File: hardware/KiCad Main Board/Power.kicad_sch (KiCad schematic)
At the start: 53 parts, among them J7 BATT_CONN, Q2 AO3401A, Q3 AO3400A, Q4 AO3400A, Q5 AO3400A, Q6 AO3400A, U10 LM5157RTER, U13 NCP1117-1.8_SOT223, U2 S-8252ACP-M6T1U, U3 NCP1117-3.3_SOT223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

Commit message: working on PCB
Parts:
- removed D5, D6, D7: 30BQ040TRPBF, symbol Device:D_Small
- removed J7: BATT_CONN, symbol Connector:Conn_01x03_Socket
- removed R10, R12: 0, symbol Device:R
- added BT1: BK-18650-PC4, BK-18650-PC4:BAT_BK-18650-PC4, symbol BK-18650-PC4:BK-18650-PC4
- added D30, D54, D55: B340, Diode_SMD:D_SMC, symbol Diode:B340
- added TP5: V_CHG, symbol Connector:TestPoint
- added TP6, TP7: TestPoint, symbol Connector:TestPoint
- D26: footprint (none) -> Diode_SMD:D_0603_1608Metric_Pad1.05x0.95mm_HandSolder
- L3: footprint (none) -> Inductor_SMD:L_APV_APH0650
- R25: footprint (none) -> Resistor_SMD:R_1206_3216Metric_Pad1.30x1.75mm_HandSolder
- R26, R27, R28, R29, R30, R31, R32, R33, R34, R35, R36, R37, R38, R39, R49: footprint (none) -> Resistor_SMD:R_0603_1608Metric_Pad0.98x0.95mm_HandSolder
- U10: footprint QFN_57RTER_TEX -> LM5157:QFN_57RTER_TEX-M
- U2: footprint SOT236-A-PKG_MP006-A-P-SD-2.1_ABL -> S-8252:SOT236-A-PKG_MP006-A-P-SD-2.1_ABL
- U9: value MCP73844-840I/MS -> MCP73844-820I/MS; footprint MSOP8_MC_MCH -> MCP73844:MSOP8_MC_MCH-M
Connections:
- net 1V8_AUDIO: now also TP7.1
- net 3V3_MCU: now also TP6.1
- net 5V_USB: now also D30.2 (A)
- net GND: now also C48.1, C5.1, C50.1, C6.1
- net V_BAT: now also C5.2, C50.2, C63.2, C64.2, U13.3 (VI), U3.3 (VI)
- net V_BAT_RAW: now also BT1.1+
- net V_CHG: now also D54.1 (K), TP5.1
- net at L3.2, U10.12 (SW), U10.13 (SW)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: now also D54.2 (A)
- net at R25.2, U9.1 (SENSE): now also D55.2 (A)
- net at R31.2, R35.1: now also BT1.1-, BT1.2+
- net at C56.2, Q3.2 (S), Q5.2 (S)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: now also BT1.2-
- net at C51.2, C52.2, C58.1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: now also D30.1 (K)
- net at Q2.2 (S): now also D55.1 (K)

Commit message: all GPIO nets connected on schematic
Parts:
- added TP30: TestPoint, TestPoint:TestPoint_Pad_D1.0mm, symbol Connector:TestPoint
- TP5, TP6, TP7: footprint (none) -> TestPoint:TestPoint_Pad_D1.0mm
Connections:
- net V_BAT_RAW: now also TP30.1
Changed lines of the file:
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@@
 	)
 	(junction
+		(at 173.99 91.44)
+		(diameter 0)
+		(color 0 0 0 0)
+	)
+	(junction
 		(at 135.89 69.85)
 		(diameter 0)
@@
 	(wire
 		(pts
+			(xy 173.99 91.44) (xy 250.19 91.44)
+		)
+		(stroke
+			(width 0)
+			(type default)
+		)
+	)
+	(wire
+		(pts
 			(xy 223.52 25.4) (xy 229.87 25.4)
 		)
@@
 	(wire
 		(pts
-			(xy 142.24 91.44) (xy 250.19 91.44)
+			(xy 142.24 91.44) (xy 173.99 91.44)
 		)
 		(stroke
@@
 			)
 		)
-		(property "Footprint" ""
+		(property "Footprint" "TestPoint:TestPoint_Pad_D1.0mm"
 			(at 38.1 91.44 0)
 			(effects
@@
 			)
 		)
-		(property "Footprint" ""
+		(property "Footprint" "TestPoint:TestPoint_Pad_D1.0mm"
 			(at 267.97 52.07 0)
 			(effects
@@
 			)
 		)
-		(property "Footprint" ""
+		(property "Footprint" "TestPoint:TestPoint_Pad_D1.0mm"
 			(at 270.51 25.4 0)
 			(effects
@@
 					(unit 1)
 				)
+			)
+		)
+	)
+	(symbol
+		(lib_id "Connector:TestPoint")
+		(at 173.99 91.44 0)
+		(unit 1)
+		(exclude_from_sim no)
+		(in_bom yes)
+		(on_board yes)
+		(dnp no)
+		(property "Reference" "TP30"
+			(at 173.228 89.408 0)
+			(effects
+				(font
+					(size 1.27 1.27)
+				)
+				(justify right)
+			)
+		)
+		(property "Value" "TestPoint"
+			(at 173.228 87.376 0)
+			(effects
+				(font
+					(size 1.27 1.27)
+				)
+				(justify right)
+			)
+		)
+		(property "Footprint" "TestPoint:TestPoint_Pad_D1.0mm"
+			(at 179.07 91.44 0)
+			(effects
+				(font
+					(size 1.27 1.27)
+				)
+				(hide yes)
+			)
+		)
+		(property "Datasheet" "~"
+			(at 179.07 91.44 0)
+			(effects
+				(font
+					(size 1.27 1.27)
+				)
+				(hide yes)
+			)
+		)
+		(property "Description" "test point"
+			(at 173.99 91.44 0)
+			(effects
+				(font
+					(size 1.27 1.27)
+				)
+				(hide yes)
+			)
+		)
+		(pin "1"
+		)
+		(instances
+			(project "OSS Radio Hardware Design"
+				(path "/fd5c68a7-f5d0-4135-a258-bde3ebf63307/c701d20d-e266-4c46-aeb3-ff3d813a359d"
+					(reference "TP30")
+					(unit 1)
+				)

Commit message: mostly designed PCB
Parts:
- removed TP6, TP7: TestPoint, TestPoint:TestPoint_Pad_D1.0mm, symbol Connector:TestPoint
- added C78: 4.7u, Capacitor_SMD:C_0603_1608Metric_Pad1.08x0.95mm_HandSolder, symbol Device:C
- D30, D54, D55: footprint Diode_SMD:D_SMC -> Diode_SMD:D_SMA
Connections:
- net 1V8_AUDIO: now also C78.2
- net GND: now also C78.1
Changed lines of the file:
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@@
 	)
 	(junction
+		(at 266.7 52.07)
+		(diameter 0)
+		(color 0 0 0 0)
+	)
+	(junction
 		(at 46.99 106.68)
 		(diameter 0)
@@
 	)
 	(junction
-		(at 36.83 69.85)
+		(at 256.54 59.69)
 		(diameter 0)
 		(color 0 0 0 0)
 	)
 	(junction
-		(at 222.25 137.16)
+		(at 36.83 69.85)
 		(diameter 0)
 		(color 0 0 0 0)
 	)
 	(junction
-		(at 262.89 52.07)
+		(at 222.25 137.16)
 		(diameter 0)
 		(color 0 0 0 0)
@@
 	)
 	(junction
-		(at 265.43 25.4)
-		(diameter 0)
-		(color 0 0 0 0)
-	)
-	(junction
 		(at 208.28 40.64)
 		(diameter 0)
@@
 	(wire
 		(pts
-			(xy 256.54 25.4) (xy 265.43 25.4)
+			(xy 256.54 25.4) (xy 267.97 25.4)
 		)
 		(stroke
@@
 	(wire
 		(pts
-			(xy 265.43 25.4) (xy 267.97 25.4)
-		)
-		(stroke
-			(width 0)
-			(type default)
-		)
-	)
-	(wire
-		(pts
 			(xy 52.07 109.22) (xy 43.18 109.22)
 		)
@@
 	(wire
 		(pts
-			(xy 256.54 52.07) (xy 262.89 52.07)
-		)
-		(stroke
-			(width 0)
-			(type default)
-		)
-	)
-	(wire
-		(pts
 			(xy 36.83 106.68) (xy 36.83 109.22)
 		)
@@
 	(wire
 		(pts
-			(xy 262.89 52.07) (xy 267.97 52.07)
+			(xy 256.54 52.07) (xy 266.7 52.07)
 		)
 		(stroke
@@
 	(wire
 		(pts
+			(xy 256.54 59.69) (xy 266.7 59.69)
+		)
+		(stroke
+			(width 0)
+			(type default)
+		)
+	)
+	(wire
+		(pts
 			(xy 69.85 55.88) (xy 68.58 55.88)
 		)
@@
 	(wire
 		(pts
+			(xy 266.7 52.07) (xy 267.97 52.07)
+		)
+		(stroke
+			(width 0)
+			(type default)
+		)
+	)
+	(wire
+		(pts
 			(xy 223.52 33.02) (xy 223.52 34.29)
 		)
@@
 	)
 	(symbol
+		(lib_id "Device:C")
+		(at 266.7 55.88 180)
+		(unit 1)
+		(exclude_from_sim no)
+		(in_bom yes)
+		(on_board yes)
+		(dnp no)
+		(fields_autoplaced yes)
+		(property "Reference" "C78"
+			(at 270.51 54.6099 0)
+			(effects
+				(font
+					(size 1.27 1.27)
+				)
+				(justify right)
+			)
+		)
+		(property "Value" "4.7u"
+			(at 270.51 57.1499 0)
+			(effects
+				(font
+					(size 1.27 1.27)
+				)
+				(justify right)
+			)
+		)
+		(property "Footprint" "Capacitor_SMD:C_0603_1608Metric_Pad1.08x0.95mm_HandSolder"
+			(at 265.7348 52.07 0)
+			(effects
+				(font
+					(size 1.27 1.27)
+				)
+				(hide yes)
+			)
+		)
+		(property "Datasheet" "~"
+			(at 266.7 55.88 0)
+			(effects
+				(font
+					(size 1.27 1.27)
+				)
+				(hide yes)
+			)
+		)
+		(property "Description" "Unpolarized capacitor"
+			(at 266.7 55.88 0)
+			(effects
+				(font
+					(size 1.27 1.27)
+				)
+				(hide yes)
+			)
+		)
+		(pin "1"
+		)
+		(pin "2"
+		)
+		(instances
+			(project "OSS Radio Hardware Design"
+				(path "/fd5c68a7-f5d0-4135-a258-bde3ebf63307/c701d20d-e266-4c46-aeb3-ff3d813a359d"
+					(reference "C78")
+					(unit 1)
+				)
+			)
+		)
+	)
+	(symbol
 		(lib_id "Device:R_Small")
 		(at 149.86 52.07 0)
@@
 	)
 	(symbol
-		(lib_id "Connector:TestPoint")
-		(at 262.89 52.07 0)
-		(unit 1)
-		(exclude_from_sim no)
-		(in_bom yes)
-		(on_board yes)
-		(dnp no)
-		(fields_autoplaced yes)
-		(property "Reference" "TP7"
-			(at 265.43 47.4979 0)
-			(effects
-				(font
-					(size 1.27 1.27)
-				)
-				(justify left)
-			)
-		)
-		(property "Value" "TestPoint"
-			(at 265.43 50.0379 0)
-			(effects
-				(font
-					(size 1.27 1.27)
-				)
-				(justify left)
-			)
-		)
-		(property "Footprint" "TestPoint:TestPoint_Pad_D1.0mm"
-			(at 267.97 52.07 0)
-			(effects
-				(font
-					(size 1.27 1.27)
-				)
-				(hide yes)
-			)
-		)
-		(property "Datasheet" "~"
-			(at 267.97 52.07 0)
-			(effects
-				(font
-					(size 1.27 1.27)
-				)
-				(hide yes)
-			)
-		)
-		(property "Description" "test point"
-			(at 262.89 52.07 0)
-			(effects
-				(font
-					(size 1.27 1.27)
-				)
-				(hide yes)
-			)
-		)
-		(pin "1"
-		)
-		(instances
-			(project "OSS Radio Hardware Design"
-				(path "/fd5c68a7-f5d0-4135-a258-bde3ebf63307/c701d20d-e266-4c46-aeb3-ff3d813a359d"
-					(reference "TP7")
-					(unit 1)
-				)
-			)
-		)
-	)
-	(symbol
 		(lib_id "Device:R_Small")
 		(at 186.69 111.76 270)
@@
 	)
 	(symbol
-		(lib_id "Connector:TestPoint")
-		(at 265.43 25.4 0)
-		(unit 1)
-		(exclude_from_sim no)
-		(in_bom yes)
-		(on_board yes)
-		(dnp no)
-		(fields_autoplaced yes)
-		(property "Reference" "TP6"
-			(at 267.97 20.8279 0)
-			(effects
-				(font
-					(size 1.27 1.27)
-				)
-				(justify left)
-			)
-		)
-		(property "Value" "TestPoint"
-			(at 267.97 23.3679 0)
-			(effects
-				(font
-					(size 1.27 1.27)
-				)
-				(justify left)
-			)
-		)
-		(property "Footprint" "TestPoint:TestPoint_Pad_D1.0mm"
-			(at 270.51 25.4 0)
-			(effects
-				(font
-					(size 1.27 1.27)
-				)
-				(hide yes)
-			)
-		)
-		(property "Datasheet" "~"
-			(at 270.51 25.4 0)
-			(effects
-				(font
-					(size 1.27 1.27)
-				)
-				(hide yes)
-			)
-		)
-		(property "Description" "test point"
-			(at 265.43 25.4 0)
-			(effects
-				(font
-					(size 1.27 1.27)
-				)
-				(hide yes)
-			)
-		)
-		(pin "1"
-		)
-		(instances
-			(project ""
-				(path "/fd5c68a7-f5d0-4135-a258-bde3ebf63307/c701d20d-e266-4c46-aeb3-ff3d813a359d"
-					(reference "TP6")
-					(unit 1)
-				)
-			)
-		)
-	)
-	(symbol
 		(lib_id "Device:R_Small")
 		(at 41.91 106.68 270)
@@
 			)
 		)
-		(property "Footprint" "Diode_SMD:D_SMC"
+		(property "Footprint" "Diode_SMD:D_SMA"
 			(at 31.75 17.145 0)
 			(effects
@@
 			)
 		)
-		(property "Footprint" "Diode_SMD:D_SMC"
+		(property "Footprint" "Diode_SMD:D_SMA"
 			(at 143.51 41.275 0)
 			(effects
@@
 			)
 		)
-		(property "Footprint" "Diode_SMD:D_SMC"
+		(property "Footprint" "Diode_SMD:D_SMA"
 			(at 96.52 86.995 0)
 			(effects

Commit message: did all the things
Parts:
- added D59: 1N4148WS, Diode_SMD:D_SOD-323, symbol Diode:1N4148WS
- added J9: Batt_Conn, TestPoint:TestPoint_2Pads_Pitch2.54mm_Drill0.8mm, symbol Connector:Conn_01x02_Pin
- BT1, C56, C57, Q3, Q4, R30, R31, R32, R33, R34, R35, U2: now not fitted
- R49: value 100 -> 1k
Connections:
- net 3V3_MCU: no longer D26.2 (A)
- net CHGR_STAT: now also D59.2 (A); no longer R49.2, U9.3 (STAT1)
- net GND: now also J9.1 (Pin_1)
- net V_BAT_RAW: now also J9.2 (Pin_2)
- net V_CHG: now also D26.2 (A)
- new net: D59.1 (K), R49.2, U9.3 (STAT1)
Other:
- moved on the sheet: C59, R28

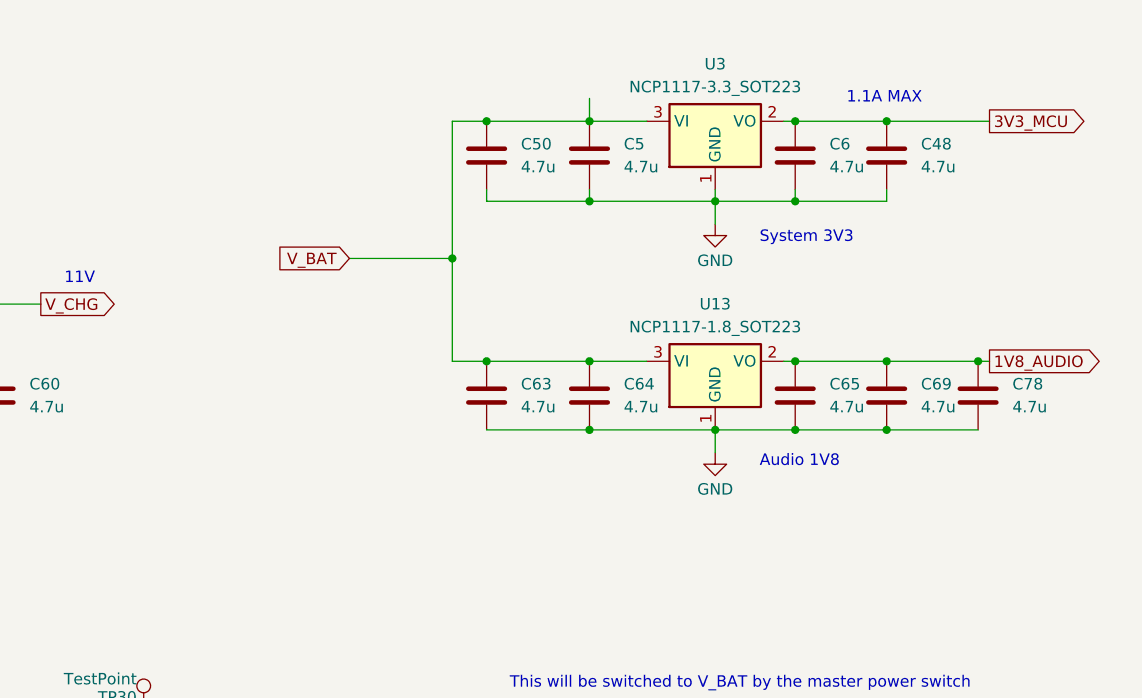
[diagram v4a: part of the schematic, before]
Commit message: changed 3V3 regulator from LDO to switching, updated PCB and minor PCB changes
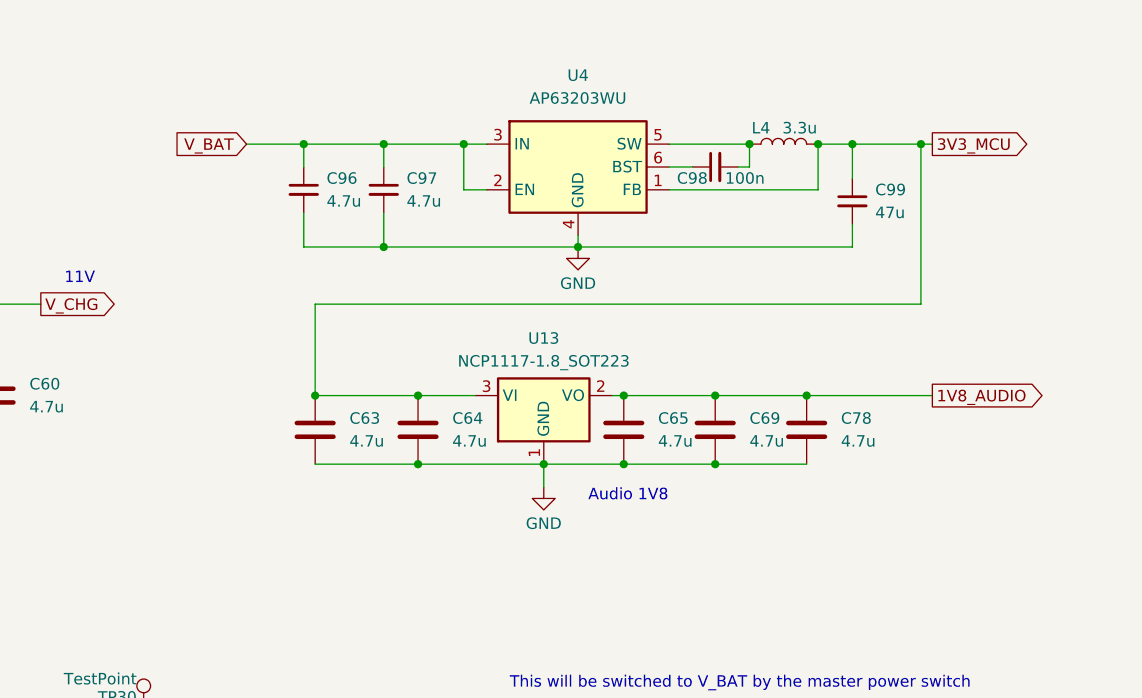
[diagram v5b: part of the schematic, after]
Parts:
- removed C48, C5, C50, C6: 4.7u, Capacitor_SMD:C_0603_1608Metric_Pad1.08x0.95mm_HandSolder, symbol Device:C
- removed U3: NCP1117-3.3_SOT223, Package_TO_SOT_SMD:SOT-223-3_TabPin2, symbol Regulator_Linear:NCP1117-3.3_SOT223
- added C96, C97: 4.7u, Capacitor_SMD:C_0603_1608Metric_Pad1.08x0.95mm_HandSolder, symbol Device:C_Small
- added C98: 100n, Capacitor_SMD:C_0603_1608Metric_Pad1.08x0.95mm_HandSolder, symbol Device:C_Small
- added C99: 47u, Capacitor_SMD:C_1206_3216Metric_Pad1.33x1.80mm_HandSolder, symbol Device:C_Small
- added L4: 3.3u, Inductor_SMD:L_0805_2012Metric_Pad1.15x1.40mm_HandSolder, symbol Device:L
- added U4: AP63203WU, Package_TO_SOT_SMD:TSOT-23-6, symbol Regulator_Switching:AP63203WU
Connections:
- net 3V3_MCU: now also C63.2, C64.2, U13.3 (VI), C99.1, L4.2, U4.1 (FB)
- net GND: now also C96.2, C97.2, C99.2, U4.4 (GND)
- net V_BAT: now also C96.1, C97.1, U4.2 (EN), U4.3 (IN); no longer C63.2, C64.2, U13.3 (VI)
- new net: C98.1, U4.6 (BST)
- new net: C98.2, L4.1, U4.5 (SW)
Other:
- note removed: "1.1A MAX"
- note removed: "System 3V3"
- moved on the sheet: C63, C64, C65, C69, C78, U13

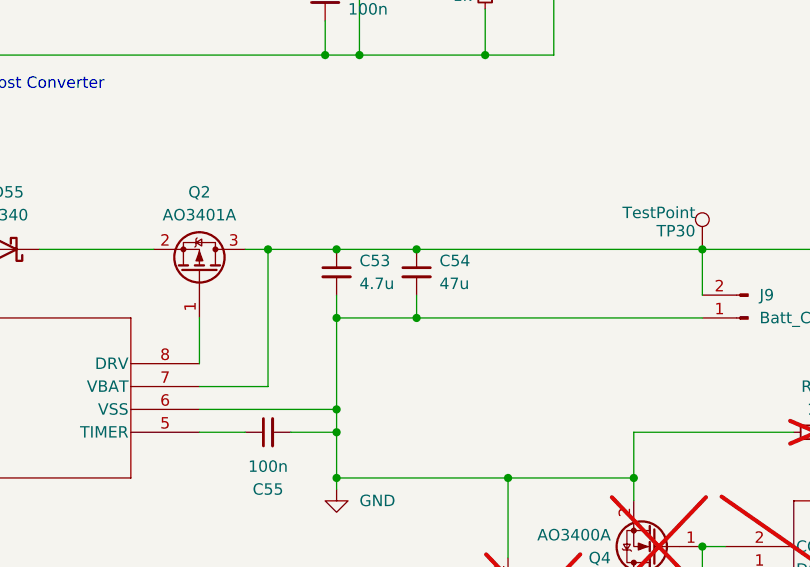
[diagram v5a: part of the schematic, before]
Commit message: changed charge output 47uF cap to 4.7uF due to size/voltage constraints
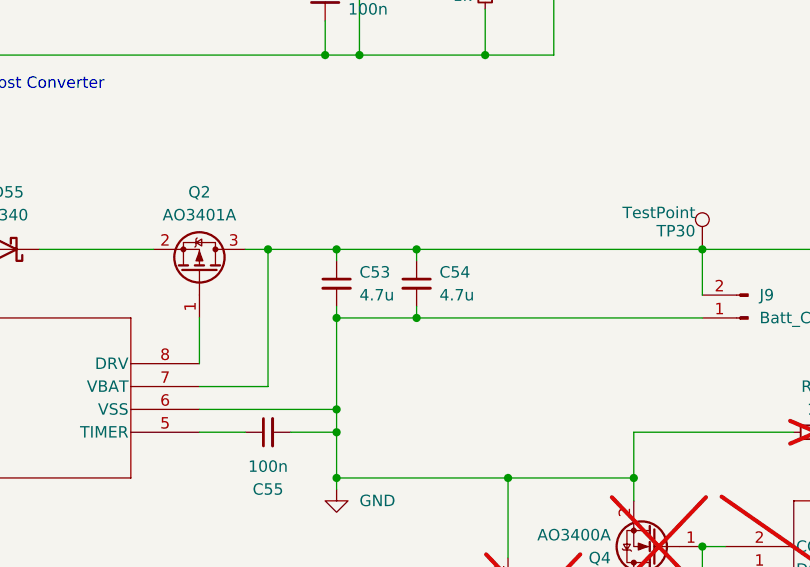
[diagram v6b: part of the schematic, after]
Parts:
- C54: value 47u -> 4.7u; footprint Capacitor_SMD:C_1206_3216Metric_Pad1.33x1.80mm_HandSolder -> Capacitor_SMD:C_0603_1608Metric_Pad1.08x0.95mm_HandSolder
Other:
- moved on the sheet: C53
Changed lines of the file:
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@@
 	)
 	(junction
-		(at 142.24 91.44)
-		(diameter 0)
-		(color 0 0 0 0)
-	)
-	(junction
 		(at 43.18 129.54)
 		(diameter 0)
@@
 	)
 	(junction
+		(at 142.24 91.44)
+		(diameter 0)
+		(color 0 0 0 0)
+	)
+	(junction
 		(at 149.86 69.85)
 		(diameter 0)
@@
 	(wire
 		(pts
-			(xy 133.35 96.52) (xy 133.35 99.06)
+			(xy 133.35 97.79) (xy 133.35 99.06)
 		)
 		(stroke
@@
 	(wire
 		(pts
+			(xy 142.24 92.71) (xy 142.24 91.44)
+		)
+		(stroke
+			(width 0)
+			(type default)
+		)
+	)
+	(wire
+		(pts
 			(xy 276.86 140.97) (xy 276.86 144.78)
 		)
@@
 	(wire
 		(pts
+			(xy 133.35 92.71) (xy 133.35 91.44)
+		)
+		(stroke
+			(width 0)
+			(type default)
+		)
+	)
+	(wire
+		(pts
 			(xy 132.08 55.88) (xy 125.73 55.88)
 		)
@@
 	(wire
 		(pts
-			(xy 142.24 96.52) (xy 142.24 99.06)
+			(xy 142.24 97.79) (xy 142.24 99.06)
 		)
 		(stroke
@@
 	(wire
 		(pts
-			(xy 142.24 99.06) (xy 133.35 99.06)
+			(xy 142.24 91.44) (xy 173.99 91.44)
 		)
 		(stroke
@@
 	(wire
 		(pts
-			(xy 118.11 109.22) (xy 133.35 109.22)
+			(xy 142.24 99.06) (xy 133.35 99.06)
 		)
 		(stroke
@@
 	(wire
 		(pts
-			(xy 260.35 27.94) (xy 252.73 27.94)
+			(xy 118.11 109.22) (xy 133.35 109.22)
 		)
 		(stroke
@@
 	(wire
 		(pts
-			(xy 217.17 142.24) (xy 222.25 142.24)
+			(xy 260.35 27.94) (xy 252.73 27.94)
 		)
 		(stroke
@@
 	(wire
 		(pts
-			(xy 176.53 127) (xy 176.53 138.43)
+			(xy 217.17 142.24) (xy 222.25 142.24)
 		)
 		(stroke
@@
 	(wire
 		(pts
-			(xy 142.24 91.44) (xy 173.99 91.44)
+			(xy 176.53 127) (xy 176.53 138.43)
 		)
 		(stroke
@@
 	(symbol
 		(lib_id "Device:C_Small")
-		(at 133.35 93.98 0)
+		(at 133.35 95.25 0)
 		(unit 1)
 		(exclude_from_sim no)
@@
 		(fields_autoplaced yes)
 		(property "Reference" "C53"
-			(at 135.89 92.7162 0)
+			(at 135.89 93.9862 0)
 			(effects
 				(font
@@
 		)
 		(property "Value" "4.7u"
-			(at 135.89 95.2562 0)
+			(at 135.89 96.5262 0)
 			(effects
 				(font
@@
 		)
 		(property "Footprint" "Capacitor_SMD:C_0603_1608Metric_Pad1.08x0.95mm_HandSolder"
-			(at 133.35 93.98 0)
+			(at 133.35 95.25 0)
 			(effects
 				(font
@@
 		)
 		(property "Datasheet" "~"
-			(at 133.35 93.98 0)
+			(at 133.35 95.25 0)
 			(effects
 				(font
@@
 		)
 		(property "Description" "Unpolarized capacitor, small symbol"
-			(at 133.35 93.98 0)
+			(at 133.35 95.25 0)
 			(effects
 				(font
@@
 	)
 	(symbol
+		(lib_id "Device:C_Small")
+		(at 142.24 95.25 0)
+		(unit 1)
+		(exclude_from_sim no)
+		(in_bom yes)
+		(on_board yes)
+		(dnp no)
+		(fields_autoplaced yes)
+		(property "Reference" "C54"
+			(at 144.78 93.9862 0)
+			(effects
+				(font
+					(size 1.27 1.27)
+				)
+				(justify left)
+			)
+		)
+		(property "Value" "4.7u"
+			(at 144.78 96.5262 0)
+			(effects
+				(font
+					(size 1.27 1.27)
+				)
+				(justify left)
+			)
+		)
+		(property "Footprint" "Capacitor_SMD:C_0603_1608Metric_Pad1.08x0.95mm_HandSolder"
+			(at 142.24 95.25 0)
+			(effects
+				(font
+					(size 1.27 1.27)
+				)
+				(hide yes)
+			)
+		)
+		(property "Datasheet" "~"
+			(at 142.24 95.25 0)
+			(effects
+				(font
+					(size 1.27 1.27)
+				)
+				(hide yes)
+			)
+		)
+		(property "Description" "Unpolarized capacitor, small symbol"
+			(at 142.24 95.25 0)
+			(effects
+				(font
+					(size 1.27 1.27)
+				)
+				(hide yes)
+			)
+		)
+		(pin "1"
+		)
+		(pin "2"
+		)
+		(instances
+			(project "OSS Radio Hardware Design"
+				(path "/fd5c68a7-f5d0-4135-a258-bde3ebf63307/c701d20d-e266-4c46-aeb3-ff3d813a359d"
+					(reference "C54")
+					(unit 1)
+				)
+			)
+		)
+	)
+	(symbol
 		(lib_id "Transistor_FET:AO3400A")
 		(at 154.94 130.81 180)
@@
 					(unit 1)
 				)
-			)
-		)
-	)
-	(symbol
-		(lib_id "Device:C_Small")
-		(at 142.24 93.98 0)
-		(unit 1)
-		(exclude_from_sim no)
-		(in_bom yes)
-		(on_board yes)
-		(dnp no)
-		(fields_autoplaced yes)
-		(property "Reference" "C54"
-			(at 144.78 92.7162 0)
-			(effects
-				(font
-					(size 1.27 1.27)
-				)
-				(justify left)
-			)
-		)
-		(property "Value" "47u"
-			(at 144.78 95.2562 0)
-			(effects
-				(font
-					(size 1.27 1.27)
-				)
-				(justify left)
-			)
-		)
-		(property "Footprint" "Capacitor_SMD:C_1206_3216Metric_Pad1.33x1.80mm_HandSolder"
-			(at 142.24 93.98 0)
-			(effects
-				(font
-					(size 1.27 1.27)
-				)
-				(hide yes)
-			)
-		)
-		(property "Datasheet" "~"
-			(at 142.24 93.98 0)
-			(effects
-				(font
-					(size 1.27 1.27)
-				)
-				(hide yes)
-			)
-		)
-		(property "Description" "Unpolarized capacitor, small symbol"
-			(at 142.24 93.98 0)
-			(effects
-				(font
-					(size 1.27 1.27)
-				)
-				(hide yes)
-			)
-		)
-		(pin "1"
-		)
-		(pin "2"
-		)
-		(instances
-			(project "OSS Radio Hardware Design"
-				(path "/fd5c68a7-f5d0-4135-a258-bde3ebf63307/c701d20d-e266-4c46-aeb3-ff3d813a359d"
-					(reference "C54")
-					(unit 1)
-				)
